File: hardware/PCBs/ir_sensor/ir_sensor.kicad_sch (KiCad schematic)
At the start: 27 parts

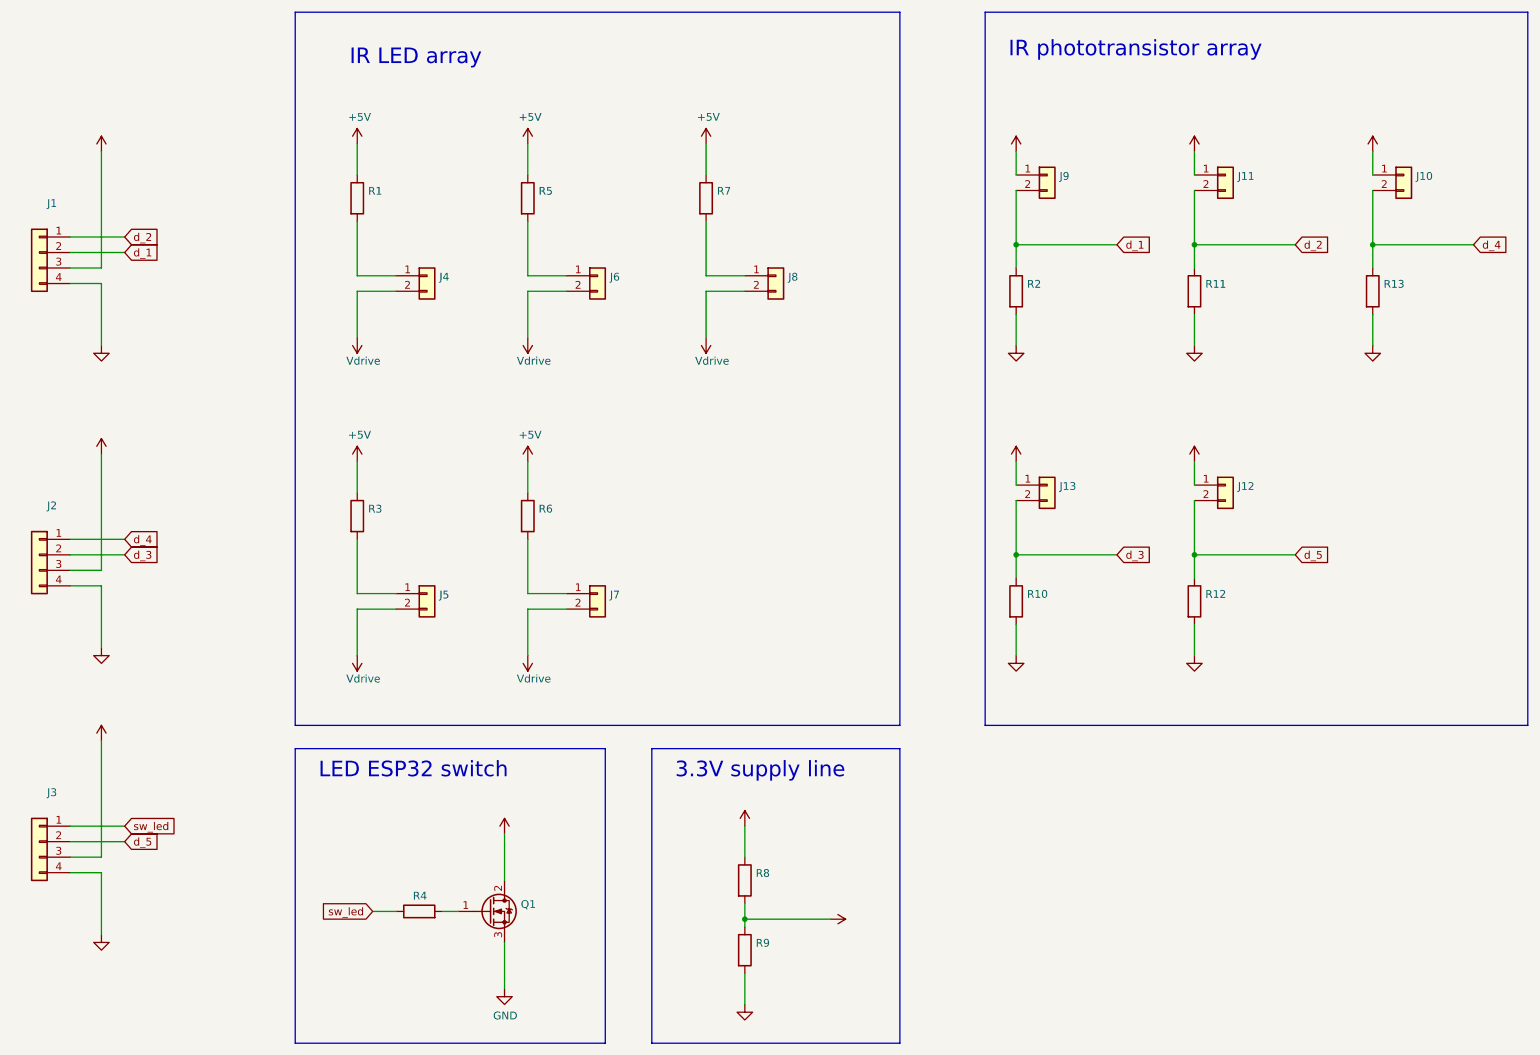
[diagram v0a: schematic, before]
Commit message: Update IR sensor to v0.4
IR sensor board updated to version 0.4:
- removed MOSFET switch;
First of all, it was supposed to be IRFL44 , L version which can be used with logic levels. But instead we put IRFZ which barely opens at 3.3 V and thus cannot be effectively used here. Moreover, during the actual usage of the board, 5V line was constantly ON and it did not cause to much of a trouble. This change is also correlated with the upcoming redesign of the main hub.
- Add additional phototransistor connector
- Add additional IR LED connector

Co-Authored-By: Andre Maia Chagas <a.maia-chagas@sussex.ac.uk>
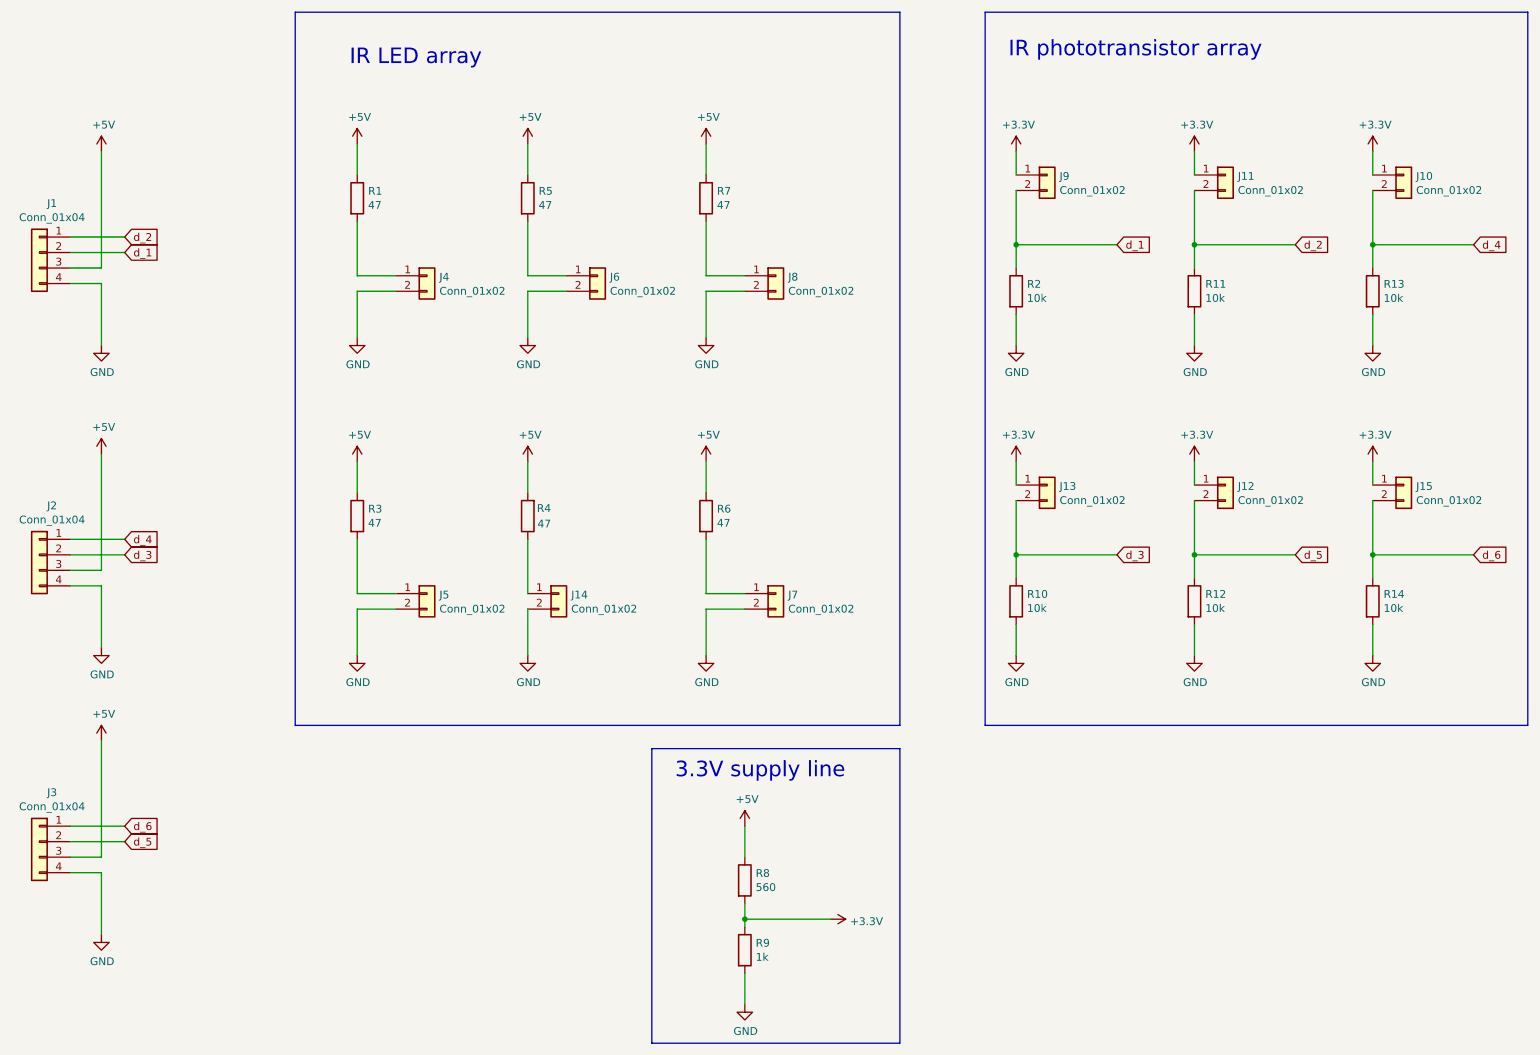
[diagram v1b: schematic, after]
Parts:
- removed Q1: (no value), symbol Transistor_FET:IRLZ44N
- added J14, J15: Conn_01x02, Connector_JST:JST_XH_B2B-XH-A_1x02_P2.50mm_Vertical, symbol Connector_Generic:Conn_01x02
- added R14: 10k, Resistor_THT:R_Box_L13.0mm_W4.0mm_P9.00mm, symbol Device:R
- J1, J2, J3: value (none) -> Conn_01x04; footprint (none) -> Connector_JST:JST_XH_B4B-XH-A_1x04_P2.50mm_Vertical
- J10, J11, J12, J13, J4, J5, J6, J7, J8, J9: value (none) -> Conn_01x02; footprint (none) -> Connector_JST:JST_XH_B2B-XH-A_1x02_P2.50mm_Vertical
- R1, R3, R4, R5, R6, R7: value (none) -> 47; footprint (none) -> Resistor_THT:R_Box_L13.0mm_W4.0mm_P9.00mm
- R10, R11, R12, R13, R2: value (none) -> 10k; footprint (none) -> Resistor_THT:R_Box_L13.0mm_W4.0mm_P9.00mm
- R8: value (none) -> 560; footprint (none) -> Resistor_THT:R_Box_L13.0mm_W4.0mm_P9.00mm
- R9: value (none) -> 1k; footprint (none) -> Resistor_THT:R_Box_L13.0mm_W4.0mm_P9.00mm
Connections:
- net Vdrive is gone; now on net GND: J4.2 (Pin_2), J5.2 (Pin_2), J6.2 (Pin_2), J7.2 (Pin_2), J8.2 (Pin_2)
- net +3V3: now also J15.1 (Pin_1)
- net +5V: now also R4.2
- net GND: now also J14.2 (Pin_2), R14.2
- net sw_led: no longer names the net of R4.1
- net sw_led: now also J14.1 (Pin_1); no longer J3.1 (Pin_1)
- new net d_6: J15.2 (Pin_2), J3.1 (Pin_1), R14.1
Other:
- note removed: "LED ESP32 switch"
- moved on the sheet: J7, R4, R6
